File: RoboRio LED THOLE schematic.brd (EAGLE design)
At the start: 18.7 x 74.9 mm, 50 parts

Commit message: Add files via upload
Matt and Jordan RoboRio LED project
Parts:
- D1, D10, D11, D12, D13, D14, D15, D16, D17, D18, D19, D2, D20, D3, D4, D5, D6, D7, D8, D9: device LilyPad-Wearables:LED-1206 -> SparkFun-LED:LTE-302
- R1, R10, R11, R12, R13, R14, R15, R16, R17, R18, R19, R2, R20, R3, R4, R5, R6, R7, R8, R9: device SparkFun-Passives:0603-RES -> SparkFun-Passives:AXIAL-0.3-KIT
- moved D10 81.8 mm to (88.9, 49.5), turned to 180 degrees
- moved D12 81.8 mm to (88.9, 41.9), turned to 180 degrees
- moved D14 81.8 mm to (88.9, 34.3), turned to 180 degrees
- moved D16 81.8 mm to (88.9, 26.7), turned to 180 degrees
- moved D18 81.8 mm to (88.9, 19.1), turned to 180 degrees
- moved D2 81.8 mm to (88.9, 80.0), turned to 180 degrees
- moved D20 81.8 mm to (88.9, 11.4), turned to 180 degrees
- moved D4 81.8 mm to (88.9, 72.4), turned to 180 degrees
- moved D6 81.8 mm to (88.9, 64.8), turned to 180 degrees
- moved D8 81.8 mm to (88.9, 57.1), turned to 180 degrees
- moved J1 81.4 mm to (97.8, 77.5)
- moved J10 81.4 mm to (97.8, 8.89)
- moved J2 81.4 mm to (97.8, 69.8)
- moved J3 81.4 mm to (97.8, 62.2)
- moved J4 81.4 mm to (97.8, 54.6)
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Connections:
- net N$1: now also R1.P$1; no longer R1.1
- net N$10: now also R7.P$1; no longer R7.1
- net N$11: now also R8.P$2; no longer R8.2
- net N$12: now also R7.P$2; no longer R7.2
- net N$13: now also R9.P$1; no longer R9.1
- net N$14: now also R10.P$2; no longer R10.2
- net N$15: now also R9.P$2; no longer R9.2
- net N$16: now also R11.P$1; no longer R11.1
- net N$17: now also R12.P$2; no longer R12.2
- net N$18: now also R11.P$2; no longer R11.2
- net N$19: now also R13.P$1; no longer R13.1
- net N$2: now also R1.P$2; no longer R1.2
- net N$20: now also R14.P$2; no longer R14.2
- net N$21: now also R13.P$2; no longer R13.2
- net N$22: now also R15.P$1; no longer R15.1
- net N$23: now also R16.P$2; no longer R16.2
- net N$24: now also R15.P$2; no longer R15.2
- net N$25: now also R17.P$1; no longer R17.1
- net N$26: now also R18.P$2; no longer R18.2
- net N$27: now also R17.P$2; no longer R17.2
- net N$28: now also R19.P$1; no longer R19.1
- net N$29: now also R20.P$2; no longer R20.2
- net N$3: now also R3.P$1; no longer R3.1
- net N$30: now also R19.P$2; no longer R19.2
- net N$4: now also R2.P$2; no longer R2.2
- net N$5: now also R4.P$2; no longer R4.2
- net N$6: now also R3.P$2; no longer R3.2
- net N$7: now also R5.P$1; no longer R5.1
- net N$8: now also R6.P$2; no longer R6.2
- net N$9: now also R5.P$2; no longer R5.2
- net S: now also R2.P$1; no longer R2.1
- net S1: now also R4.P$1; no longer R4.1
- net S2: now also R6.P$1; no longer R6.1
- net S3: now also R8.P$1; no longer R8.1
- net S4: now also R10.P$1; no longer R10.1
- net S5: now also R12.P$1; no longer R12.1
- net S6: now also R14.P$1; no longer R14.1
- net S7: now also R16.P$1; no longer R16.1
- net S8: now also R18.P$1; no longer R18.1
- net S9: now also R20.P$1; no longer R20.1
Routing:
- net S8: track 12.8 -> 0.00 mm
- net S5: track 12.8 -> 0.00 mm
- net S2: track 12.8 -> 0.00 mm
- net S7: track 12.8 -> 0.00 mm
- net S4: track 12.8 -> 0.00 mm
- net S1: track 12.8 -> 0.00 mm
- net S9: track 12.8 -> 0.00 mm
- net S6: track 12.7 -> 0.00 mm
- net S: track 12.7 -> 0.00 mm
- net S3: track 12.7 -> 0.00 mm
- net GND8: track 8.20 -> 0.00 mm
- net GND5: track 8.20 -> 0.00 mm
- net GND2: track 8.20 -> 0.00 mm
- net GND: track 8.07 -> 0.00 mm
- net GND6: track 8.07 -> 0.00 mm
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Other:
- board size 18.7 x 74.9 mm -> 27.6 x 78.7 mm

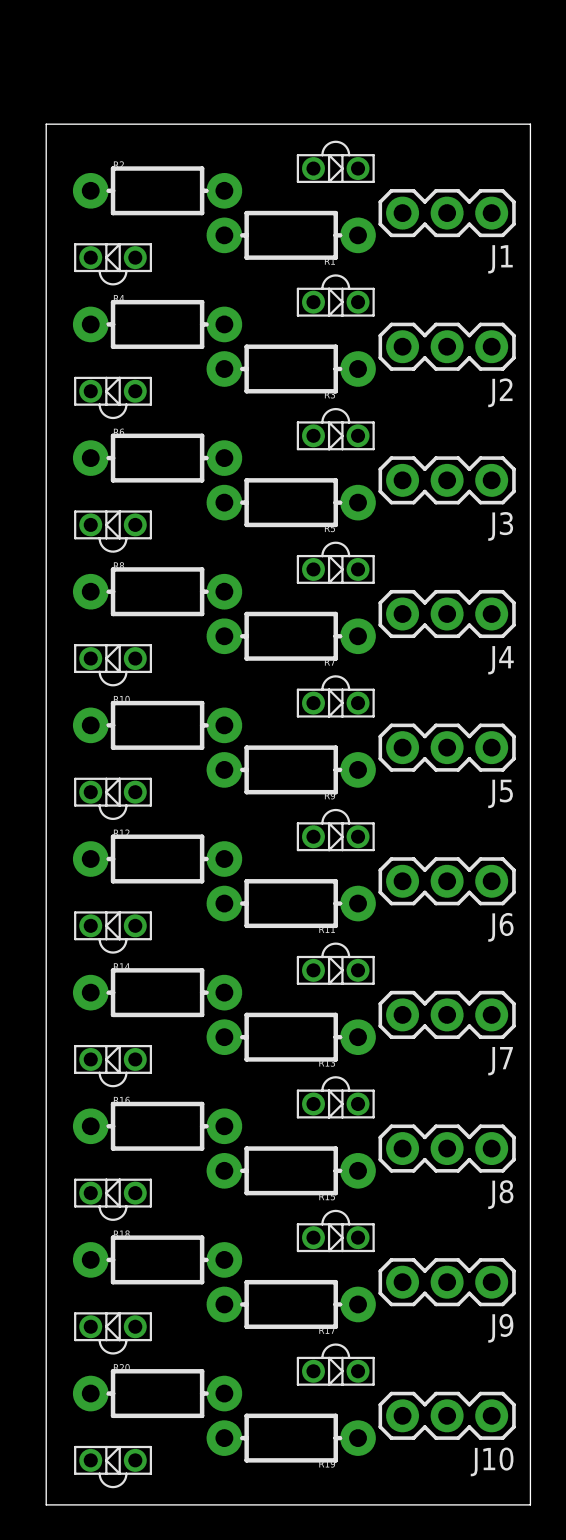
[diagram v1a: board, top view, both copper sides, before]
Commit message: Routed the through hold board. Change LED component to indicate true component size
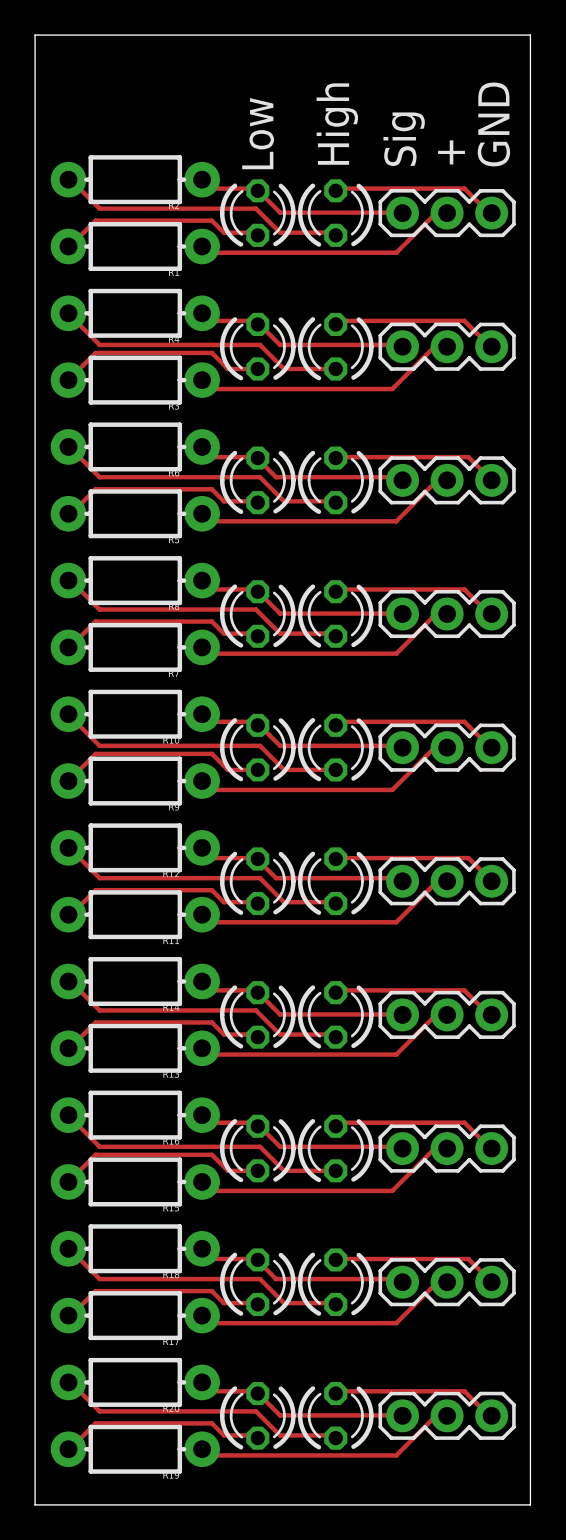
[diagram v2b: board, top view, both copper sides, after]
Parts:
- removed D1, D10, D11, D12, D13, D14, D15, D16, D17, D18, D19, D2, D20, D3, D4, D5, D6, D7, D8, D9: (no value), SparkFun-LED:LTE-302
- added LED1, LED10, LED11, LED12, LED13, LED14, LED15, LED16, LED17, LED18, LED19, LED2, LED20, LED3, LED4, LED5, LED6, LED7, LED8, LED9: (no value), led:LED3MM
- moved R1 8.91 mm to (77.5, 75.6)
- moved R11 8.91 mm to (77.5, 37.5)
- moved R13 8.91 mm to (77.5, 29.8)
- moved R15 8.91 mm to (77.5, 22.2)
- moved R17 8.91 mm to (77.5, 14.6)
- moved R19 8.91 mm to (77.5, 6.99)
- moved R3 8.91 mm to (77.5, 67.9)
- moved R5 8.91 mm to (77.5, 60.3)
- moved R7 8.91 mm to (77.5, 52.7)
- moved R9 8.91 mm to (77.5, 45.1)
- moved R10 1.42 mm to (77.5, 48.9), turned to 180 degrees
- moved R2 1.42 mm to (77.5, 79.4), turned to 180 degrees
- moved R6 1.42 mm to (77.5, 64.1), turned to 180 degrees
- moved R16 1.42 mm to (77.5, 26.0), turned to 180 degrees
- moved R20 1.42 mm to (77.5, 10.8), turned to 180 degrees
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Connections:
- net GND: now also LED2.K; no longer D2.C
- net GND1: now also LED4.K; no longer D4.C
- net GND2: now also LED6.K; no longer D6.C
- net GND3: now also LED8.K; no longer D8.C
- net GND4: now also LED10.K; no longer D10.C
- net GND5: now also LED12.K; no longer D12.C
- net GND6: now also LED14.K; no longer D14.C
- net GND7: now also LED16.K; no longer D16.C
- net GND8: now also LED18.K; no longer D18.C
- net GND9: now also LED20.K; no longer D20.C
- net N$11: now also LED8.A; no longer D8.A
- net N$12: now also LED7.A; no longer D7.A
- net N$14: now also LED10.A; no longer D10.A
- net N$15: now also LED9.A; no longer D9.A
- net N$17: now also LED12.A; no longer D12.A
- net N$18: now also LED11.A; no longer D11.A
- net N$2: now also LED1.A; no longer D1.A
- net N$20: now also LED14.A; no longer D14.A
- net N$21: now also LED13.A; no longer D13.A
- net N$23: now also LED16.A; no longer D16.A
- net N$24: now also LED15.A; no longer D15.A
- net N$26: now also LED18.A; no longer D18.A
- net N$27: now also LED17.A; no longer D17.A
- net N$29: now also LED20.A; no longer D20.A
- net N$30: now also LED19.A; no longer D19.A
- net N$4: now also LED2.A; no longer D2.A
- net N$5: now also LED4.A; no longer D4.A
- net N$6: now also LED3.A; no longer D3.A
- net N$8: now also LED6.A; no longer D6.A
- net N$9: now also LED5.A; no longer D5.A
- net S: now also LED1.K; no longer D1.C
- net S1: now also LED3.K; no longer D3.C
- net S2: now also LED5.K; no longer D5.C
- net S3: now also LED7.K; no longer D7.C
- net S4: now also LED9.K; no longer D9.C
- net S5: now also LED11.K; no longer D11.C
- net S6: now also LED13.K; no longer D13.C
- net S7: now also LED15.K; no longer D15.C
- net S8: now also LED17.K; no longer D17.C
- net S9: now also LED19.K; no longer D19.C
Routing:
- net N$14: track 0.00 -> 16.6 mm
- net N$23: track 0.00 -> 16.6 mm
- net N$5: track 0.00 -> 16.6 mm
- net N$4: track 0.00 -> 16.5 mm
- net N$29: track 0.00 -> 16.5 mm
- net N$20: track 0.00 -> 16.5 mm
- net N$11: track 0.00 -> 16.5 mm
- net N$8: track 0.00 -> 16.5 mm
- net N$26: track 0.00 -> 16.5 mm
- net N$17: track 0.00 -> 16.5 mm
- net N$13: track 0.00 -> 15.2 mm
- net N$22: track 0.00 -> 15.2 mm
- net N$3: track 0.00 -> 15.2 mm
- net N$7: track 0.00 -> 15.1 mm
- net N$25: track 0.00 -> 15.1 mm
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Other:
- board size 27.6 x 78.7 mm -> 28.2 x 83.8 mm
- board text added: "+"
- board text added: "GND"
- board text added: "High"
- board text added: "Low"
- board text added: "Sig"
